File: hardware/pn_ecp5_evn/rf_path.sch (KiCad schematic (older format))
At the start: 37 parts, among them J701 Conn_Coaxial, J702 Conn_Coaxial, J703 Conn_Coaxial, U701 SYM-63LH+, U702 ADG621, U703 OPA2211

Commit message: first pass footprint assignment on pn r0
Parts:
- C701, C702, C703, C704, C705, C706, C707, C708, C709, C710, C711, C712: footprint (none) -> Capacitor_SMD:C_0402_1005Metric
- J701, J702, J703: footprint (none) -> Connector_Coaxial:U.FL_Hirose_U.FL-R-SMT-1_Vertical
- R701, R702, R703, R704, R705, R706, R707, R708, R709, R710, R711, R712, R713, R714, R715, R716, R717, R718, R719: footprint (none) -> Resistor_SMD:R_0402_1005Metric
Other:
- moved on the sheet: U702A, U702C
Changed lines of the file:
@@
 F 0 "C701" V 1621 3200 50  0000 C CNN
 F 1 "C_Small" V 1712 3200 50  0000 C CNN
-F 2 "" H 1850 3200 50  0001 C CNN
+F 2 "Capacitor_SMD:C_0402_1005Metric" H 1850 3200 50  0001 C CNN
 F 3 "~" H 1850 3200 50  0001 C CNN
 	1    1850 3200
@@
 F 0 "C703" H 2658 4354 50  0000 R CNN
 F 1 "DNI" H 2658 4445 50  0000 R CNN
-F 2 "" H 2750 4400 50  0001 C CNN
+F 2 "Capacitor_SMD:C_0402_1005Metric" H 2750 4400 50  0001 C CNN
 F 3 "~" H 2750 4400 50  0001 C CNN
 	1    2750 4400
@@
 F 0 "C702" H 2658 4146 50  0000 R CNN
 F 1 "DNI" H 2658 4055 50  0000 R CNN
-F 2 "" H 2750 4100 50  0001 C CNN
+F 2 "Capacitor_SMD:C_0402_1005Metric" H 2750 4100 50  0001 C CNN
 F 3 "~" H 2750 4100 50  0001 C CNN
 	1    2750 4100
@@
 F 0 "R702" H 4309 5796 50  0000 L CNN
 F 1 "R_Small" H 4309 5705 50  0000 L CNN
-F 2 "" H 4250 5750 50  0001 C CNN
+F 2 "Resistor_SMD:R_0402_1005Metric" H 4250 5750 50  0001 C CNN
 F 3 "~" H 4250 5750 50  0001 C CNN
 	1    4250 5750
@@
 F 0 "C710" H 4908 6154 50  0000 R CNN
 F 1 "C_Small" H 4908 6245 50  0000 R CNN
-F 2 "" H 5000 6200 50  0001 C CNN
+F 2 "Capacitor_SMD:C_0402_1005Metric" H 5000 6200 50  0001 C CNN
 F 3 "~" H 5000 6200 50  0001 C CNN
 	1    5000 6200
@@
 F 0 "C709" H 4408 6154 50  0000 R CNN
 F 1 "C_Small" H 4408 6245 50  0000 R CNN
-F 2 "" H 4500 6200 50  0001 C CNN
+F 2 "Capacitor_SMD:C_0402_1005Metric" H 4500 6200 50  0001 C CNN
 F 3 "~" H 4500 6200 50  0001 C CNN
 	1    4500 6200
@@
 F 0 "C708" H 4358 7154 50  0000 R CNN
 F 1 "C_Small" H 4358 7245 50  0000 R CNN
-F 2 "" H 4450 7200 50  0001 C CNN
+F 2 "Capacitor_SMD:C_0402_1005Metric" H 4450 7200 50  0001 C CNN
 F 3 "~" H 4450 7200 50  0001 C CNN
 	1    4450 7200
@@
 F 0 "R719" V 8254 2450 50  0000 C CNN
 F 1 "R_Small" V 8345 2450 50  0000 C CNN
-F 2 "" H 8450 2450 50  0001 C CNN
+F 2 "Resistor_SMD:R_0402_1005Metric" H 8450 2450 50  0001 C CNN
 F 3 "~" H 8450 2450 50  0001 C CNN
 	1    8450 2450
@@
 F 0 "R701" H 3791 2804 50  0000 R CNN
 F 1 "R_Small" H 3791 2895 50  0000 R CNN
-F 2 "" H 3850 2850 50  0001 C CNN
+F 2 "Resistor_SMD:R_0402_1005Metric" H 3850 2850 50  0001 C CNN
 F 3 "~" H 3850 2850 50  0001 C CNN
 	1    3850 2850
@@
 F 0 "J702" H 4300 2325 50  0000 L CNN
 F 1 "Conn_Coaxial" H 4300 2234 50  0000 L CNN
-F 2 "" H 4200 2350 50  0001 C CNN
+F 2 "Connector_Coaxial:U.FL_Hirose_U.FL-R-SMT-1_Vertical" H 4200 2350 50  0001 C CNN
 F 3 " ~" H 4200 2350 50  0001 C CNN
 	1    4200 2350
@@
 F 0 "R716" V 8054 4200 50  0000 C CNN
 F 1 "R_Small" V 8145 4200 50  0000 C CNN
-F 2 "" H 8250 4200 50  0001 C CNN
+F 2 "Resistor_SMD:R_0402_1005Metric" H 8250 4200 50  0001 C CNN
 F 3 "~" H 8250 4200 50  0001 C CNN
 	1    8250 4200
@@
 F 0 "R714" V 7754 4500 50  0000 C CNN
 F 1 "R_Small" V 7845 4500 50  0000 C CNN
-F 2 "" H 7950 4500 50  0001 C CNN
+F 2 "Resistor_SMD:R_0402_1005Metric" H 7950 4500 50  0001 C CNN
 F 3 "~" H 7950 4500 50  0001 C CNN
 	1    7950 4500
@@
 F 0 "R713" V 7554 4200 50  0000 C CNN
 F 1 "R_Small" V 7645 4200 50  0000 C CNN
-F 2 "" H 7750 4200 50  0001 C CNN
+F 2 "Resistor_SMD:R_0402_1005Metric" H 7750 4200 50  0001 C CNN
 F 3 "~" H 7750 4200 50  0001 C CNN
 	1    7750 4200
@@
 F 0 "C712" H 7258 4504 50  0000 R CNN
 F 1 "DNI" H 7258 4595 50  0000 R CNN
-F 2 "" H 7350 4550 50  0001 C CNN
+F 2 "Capacitor_SMD:C_0402_1005Metric" H 7350 4550 50  0001 C CNN
 F 3 "~" H 7350 4550 50  0001 C CNN
 	1    7350 4550
@@
 F 0 "R712" V 6304 4200 50  0000 C CNN
 F 1 "R_Small" V 6395 4200 50  0000 C CNN
-F 2 "" H 6500 4200 50  0001 C CNN
+F 2 "Resistor_SMD:R_0402_1005Metric" H 6500 4200 50  0001 C CNN
 F 3 "~" H 6500 4200 50  0001 C CNN
 	1    6500 4200
@@
 F 0 "R711" V 6254 3300 50  0000 C CNN
 F 1 "R_Small" V 6345 3300 50  0000 C CNN
-F 2 "" H 6450 3300 50  0001 C CNN
+F 2 "Resistor_SMD:R_0402_1005Metric" H 6450 3300 50  0001 C CNN
 F 3 "~" H 6450 3300 50  0001 C CNN
 	1    6450 3300
@@
 F 0 "R710" H 6091 3504 50  0000 R CNN
 F 1 "R_Small" H 6091 3595 50  0000 R CNN
-F 2 "" H 6150 3550 50  0001 C CNN
+F 2 "Resistor_SMD:R_0402_1005Metric" H 6150 3550 50  0001 C CNN
 F 3 "~" H 6150 3550 50  0001 C CNN
 	1    6150 3550
@@
 F 0 "R708" V 5654 3300 50  0000 C CNN
 F 1 "R_Small" V 5745 3300 50  0000 C CNN
-F 2 "" H 5850 3300 50  0001 C CNN
+F 2 "Resistor_SMD:R_0402_1005Metric" H 5850 3300 50  0001 C CNN
 F 3 "~" H 5850 3300 50  0001 C CNN
 	1    5850 3300
@@
 F 0 "R707" V 5346 2800 50  0000 C CNN
 F 1 "R_Small" V 5255 2800 50  0000 C CNN
-F 2 "" H 5150 2800 50  0001 C CNN
+F 2 "Resistor_SMD:R_0402_1005Metric" H 5150 2800 50  0001 C CNN
 F 3 "~" H 5150 2800 50  0001 C CNN
 	1    5150 2800
@@
 F 0 "R703" V 4254 3200 50  0000 C CNN
 F 1 "R_Small" V 4345 3200 50  0000 C CNN
-F 2 "" H 4450 3200 50  0001 C CNN
+F 2 "Resistor_SMD:R_0402_1005Metric" H 4450 3200 50  0001 C CNN
 F 3 "~" H 4450 3200 50  0001 C CNN
 	1    4450 3200
@@
 F 0 "C704" V 3429 4250 50  0000 C CNN
 F 1 "DNI" V 3338 4250 50  0000 C CNN
-F 2 "" H 3200 4250 50  0001 C CNN
+F 2 "Capacitor_SMD:C_0402_1005Metric" H 3200 4250 50  0001 C CNN
 F 3 "~" H 3200 4250 50  0001 C CNN
 	1    3200 4250
@@
 F 0 "J701" H 3628 4488 50  0000 C CNN
 F 1 "Conn_Coaxial" H 3628 4397 50  0000 C CNN
-F 2 "" H 3700 4250 50  0001 C CNN
+F 2 "Connector_Coaxial:U.FL_Hirose_U.FL-R-SMT-1_Vertical" H 3700 4250 50  0001 C CNN
 F 3 " ~" H 3700 4250 50  0001 C CNN
 	1    3700 4250
@@
 F 0 "J703" H 6600 2425 50  0000 L CNN
 F 1 "Conn_Coaxial" H 6600 2334 50  0000 L CNN
-F 2 "" H 6500 2450 50  0001 C CNN
+F 2 "Connector_Coaxial:U.FL_Hirose_U.FL-R-SMT-1_Vertical" H 6500 2450 50  0001 C CNN
 F 3 " ~" H 6500 2450 50  0001 C CNN
 	1    6500 2450
@@
 F 0 "R709" H 6091 2904 50  0000 R CNN
 F 1 "R_Small" H 6091 2995 50  0000 R CNN
-F 2 "" H 6150 2950 50  0001 C CNN
+F 2 "Resistor_SMD:R_0402_1005Metric" H 6150 2950 50  0001 C CNN
 F 3 "~" H 6150 2950 50  0001 C CNN
 	1    6150 2950
@@
 F 0 "R705" V 4946 2100 50  0000 C CNN
 F 1 "R_Small" V 4855 2100 50  0000 C CNN
-F 2 "" H 4750 2100 50  0001 C CNN
+F 2 "Resistor_SMD:R_0402_1005Metric" H 4750 2100 50  0001 C CNN
 F 3 "~" H 4750 2100 50  0001 C CNN
 	1    4750 2100
@@
 F 0 "R706" V 4554 3650 50  0000 C CNN
 F 1 "R_Small" V 4645 3650 50  0000 C CNN
-F 2 "" H 4750 3650 50  0001 C CNN
+F 2 "Resistor_SMD:R_0402_1005Metric" H 4750 3650 50  0001 C CNN
 F 3 "~" H 4750 3650 50  0001 C CNN
 	1    4750 3650
@@
 F 0 "R704" V 4254 3400 50  0000 C CNN
 F 1 "R_Small" V 4345 3400 50  0000 C CNN
-F 2 "" H 4450 3400 50  0001 C CNN
+F 2 "Resistor_SMD:R_0402_1005Metric" H 4450 3400 50  0001 C CNN
 F 3 "~" H 4450 3400 50  0001 C CNN
 	1    4450 3400
@@
 F 0 "C711" V 5379 2450 50  0000 C CNN
 F 1 "DNI" V 5288 2450 50  0000 C CNN
-F 2 "" H 5150 2450 50  0001 C CNN
+F 2 "Capacitor_SMD:C_0402_1005Metric" H 5150 2450 50  0001 C CNN
 F 3 "~" H 5150 2450 50  0001 C CNN
 	1    5150 2450
@@
 F 0 "C707" V 3779 2850 50  0000 C CNN
 F 1 "DNI" V 3688 2850 50  0000 C CNN
-F 2 "" H 3550 2850 50  0001 C CNN
+F 2 "Capacitor_SMD:C_0402_1005Metric" H 3550 2850 50  0001 C CNN
 F 3 "~" H 3550 2850 50  0001 C CNN
 	1    3550 2850
@@
 F 0 "R717" V 8254 1350 50  0000 C CNN
 F 1 "R_Small" V 8345 1350 50  0000 C CNN
-F 2 "" H 8450 1350 50  0001 C CNN
+F 2 "Resistor_SMD:R_0402_1005Metric" H 8450 1350 50  0001 C CNN
 F 3 "~" H 8450 1350 50  0001 C CNN
 	1    8450 1350
@@
 F 0 "R715" V 7954 1000 50  0000 C CNN
 F 1 "R_Small" V 8045 1000 50  0000 C CNN
-F 2 "" H 8150 1000 50  0001 C CNN
+F 2 "Resistor_SMD:R_0402_1005Metric" H 8150 1000 50  0001 C CNN
 F 3 "~" H 8150 1000 50  0001 C CNN
 	1    8150 1000
@@
 F 0 "R718" V 8254 1750 50  0000 C CNN
 F 1 "R_Small" V 8345 1750 50  0000 C CNN
-F 2 "" H 8450 1750 50  0001 C CNN
+F 2 "Resistor_SMD:R_0402_1005Metric" H 8450 1750 50  0001 C CNN
 F 3 "~" H 8450 1750 50  0001 C CNN
 	1    8450 1750
@@
 L vna:ADG621 U702
 U 3 1 5FE4205A
+P 2950 6600
+F 0 "U702" H 2550 6900 50  0000 C CNN
+F 1 "ADG621" H 2550 7000 50  0000 C CNN
+F 2 "Package_SO:MSOP-10_3x3mm_P0.5mm" H 2950 6500 50  0001 C CNN
+F 3 "https://www.analog.com/media/en/technical-documentation/data-sheets/ADG621.pdf" H 2950 6600 50  0001 C CNN
+	3    2950 6600
+	1    0    0    -1
+$EndComp
+$Comp
+L vna:ADG621 U702
+U 1 1 5FE439E0
 P 8000 2450
-F 0 "U702" H 8000 2717 50  0000 C CNN
-F 1 "ADG621" H 8000 2626 50  0000 C CNN
+F 0 "U702" H 7450 2900 50  0000 L CNN
+F 1 "ADG621" H 7450 2800 50  0000 L CNN
 F 2 "Package_SO:MSOP-10_3x3mm_P0.5mm" H 8000 2350 50  0001 C CNN
 F 3 "https://www.analog.com/media/en/technical-documentation/data-sheets/ADG621.pdf" H 8000 2450 50  0001 C CNN
-	3    8000 2450
-	1    0    0    -1
-$EndComp
-$Comp
-L vna:ADG621 U702
-U 1 1 5FE439E0
-P 2950 6600
-F 0 "U702" H 2400 7050 50  0000 L CNN
-F 1 "ADG621" H 2400 6950 50  0000 L CNN
-F 2 "Package_SO:MSOP-10_3x3mm_P0.5mm" H 2950 6500 50  0001 C CNN
-F 3 "https://www.analog.com/media/en/technical-documentation/data-sheets/ADG621.pdf" H 2950 6600 50  0001 C CNN
-	1    2950 6600
+	1    8000 2450
 	1    0    0    -1
 $EndComp
@@
 F 0 "C706" H 3208 7154 50  0000 R CNN
 F 1 "1 uF" H 3208 7245 50  0000 R CNN
-F 2 "" H 3300 7200 50  0001 C CNN
+F 2 "Capacitor_SMD:C_0402_1005Metric" H 3300 7200 50  0001 C CNN
 F 3 "~" H 3300 7200 50  0001 C CNN
 	1    3300 7200
@@
 F 0 "C705" H 3208 5954 50  0000 R CNN
 F 1 "1 uF" H 3208 6045 50  0000 R CNN
-F 2 "" H 3300 6000 50  0001 C CNN
+F 2 "Capacitor_SMD:C_0402_1005Metric" H 3300 6000 50  0001 C CNN
 F 3 "~" H 3300 6000 50  0001 C CNN
 	1    3300 6000

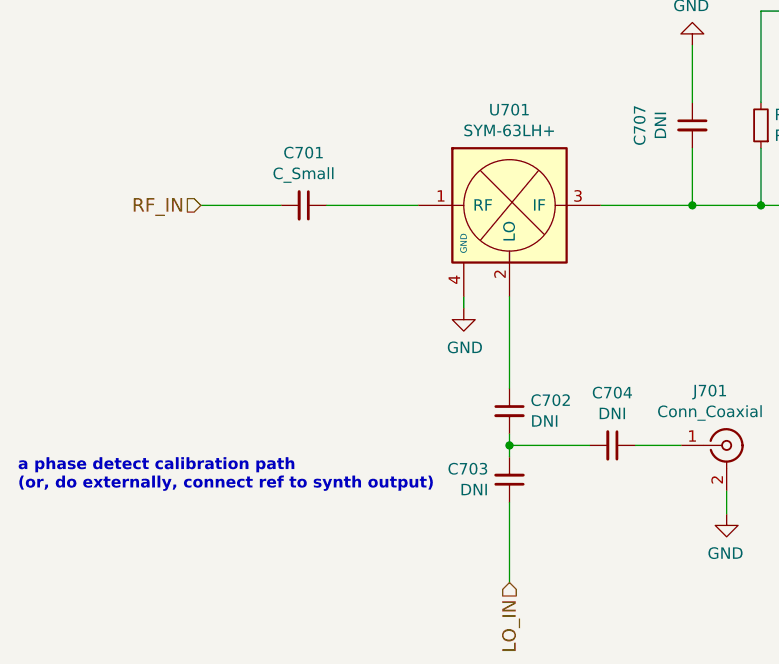
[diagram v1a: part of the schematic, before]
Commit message: started component placement on phase noise analyzer
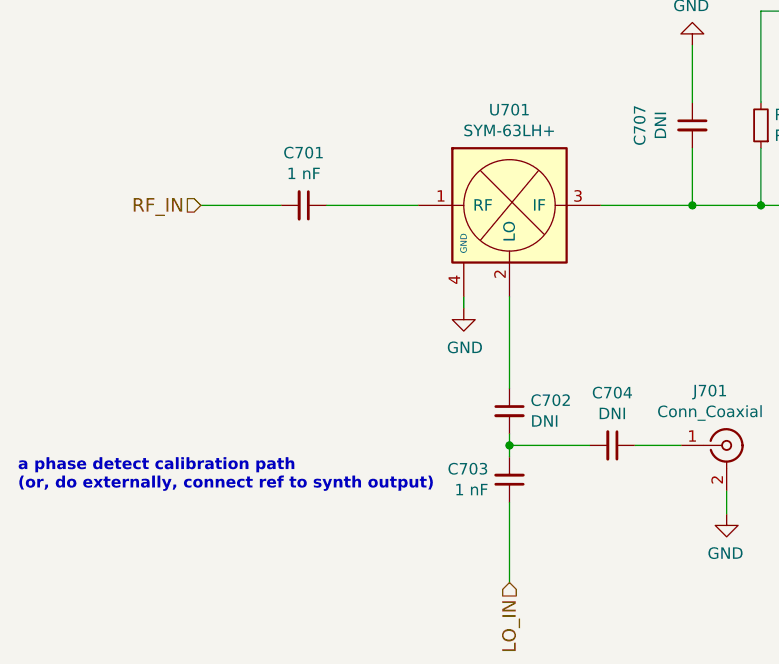
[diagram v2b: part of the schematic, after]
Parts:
- C701: value C_Small -> 1 nF
- C703: value DNI -> 1 nF
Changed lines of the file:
@@
 P 1850 3200
 F 0 "C701" V 1621 3200 50  0000 C CNN
-F 1 "C_Small" V 1712 3200 50  0000 C CNN
+F 1 "1 nF" V 1712 3200 50  0000 C CNN
 F 2 "Capacitor_SMD:C_0402_1005Metric" H 1850 3200 50  0001 C CNN
 F 3 "~" H 1850 3200 50  0001 C CNN
@@
 P 2750 4400
 F 0 "C703" H 2658 4354 50  0000 R CNN
-F 1 "DNI" H 2658 4445 50  0000 R CNN
+F 1 "1 nF" H 2658 4445 50  0000 R CNN
 F 2 "Capacitor_SMD:C_0402_1005Metric" H 2750 4400 50  0001 C CNN
 F 3 "~" H 2750 4400 50  0001 C CNN

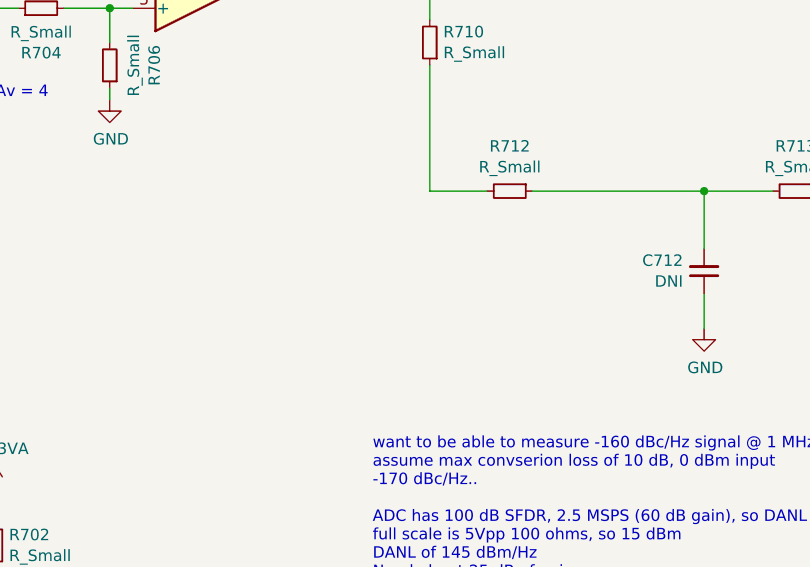
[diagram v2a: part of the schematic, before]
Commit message: work on routing phase noise downconverter
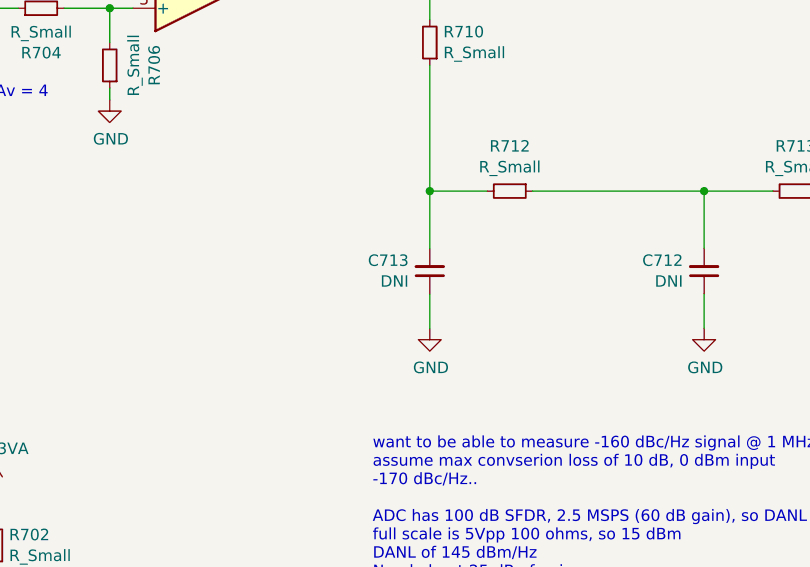
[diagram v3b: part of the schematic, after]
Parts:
- added C713: DNI, Capacitor_SMD:C_0402_1005Metric, symbol Device:C_Small
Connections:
- net GND: now also C713.1
- net at R710.1, R712.2: now also C713.2
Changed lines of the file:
@@
 Wire Wire Line
 	2950 5850 2950 6100
+Wire Wire Line
+	6150 4800 6150 4650
+$Comp
+L power:GND #PWR0305
+U 1 1 5F572A97
+P 6150 4800
+F 0 "#PWR0305" H 6150 4550 50  0001 C CNN
+F 1 "GND" H 6155 4627 50  0000 C CNN
+F 2 "" H 6150 4800 50  0001 C CNN
+F 3 "" H 6150 4800 50  0001 C CNN
+	1    6150 4800
+	1    0    0    -1
+$EndComp
+$Comp
+L Device:C_Small C713
+U 1 1 5F572A9D
+P 6150 4550
+F 0 "C713" H 6058 4504 50  0000 R CNN
+F 1 "DNI" H 6058 4595 50  0000 R CNN
+F 2 "Capacitor_SMD:C_0402_1005Metric" H 6150 4550 50  0001 C CNN
+F 3 "~" H 6150 4550 50  0001 C CNN
+	1    6150 4550
+	1    0    0    1
+$EndComp
+Wire Wire Line
+	6150 4450 6150 4200
+Connection ~ 6150 4200
 $EndSCHEMATC

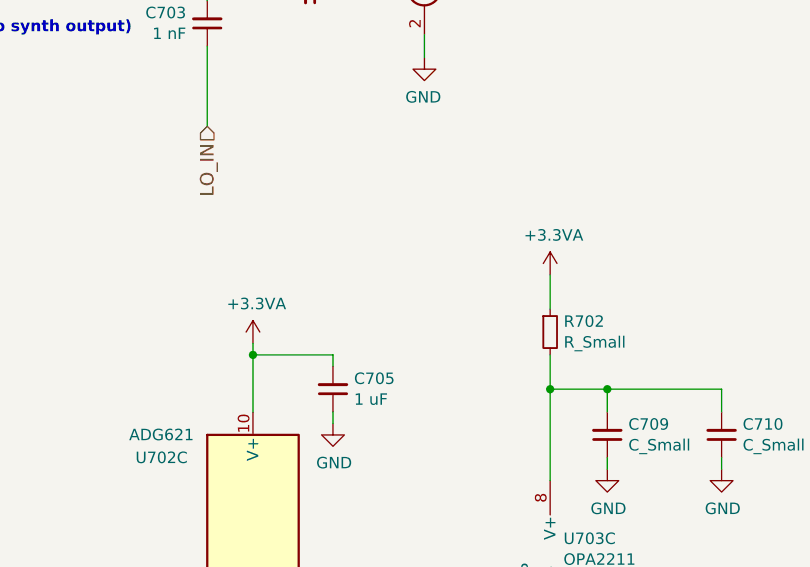
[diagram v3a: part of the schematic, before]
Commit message: layout of phase noise downconverter
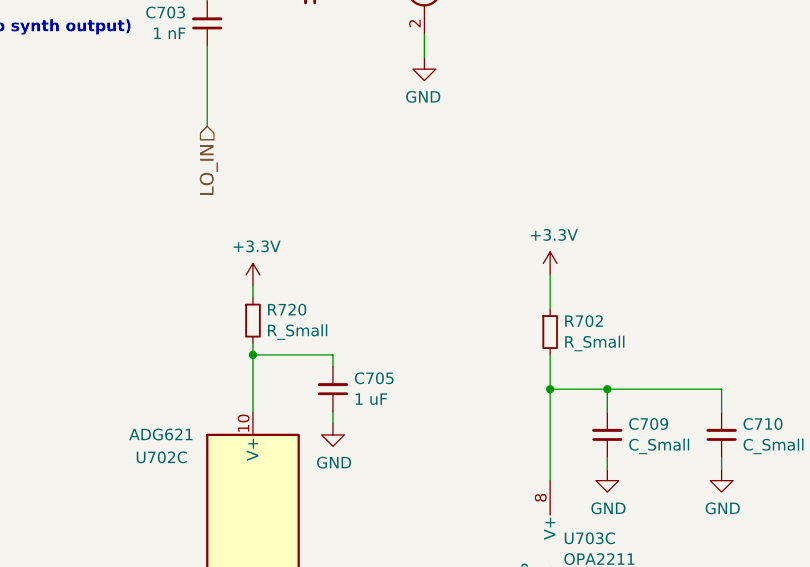
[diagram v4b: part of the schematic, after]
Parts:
- added R720: R_Small, Resistor_SMD:R_0402_1005Metric, symbol Device:R_Small
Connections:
- net +3.3VA: no longer names the net of C705.2, U702.10 (V+)
- net +3.3VA: now also R720.2; no longer R702.1
- new net +3V3: R702.1, R720.1
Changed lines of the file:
@@
 Wire Wire Line
 	4250 5500 4250 5650
-$Comp
-L power:+3.3VA #PWR0220
-U 1 1 5F8805F8
-P 4250 5500
-AR Path="/5F265927/5F8805F8" Ref="#PWR0220"  Part="1"
-AR Path="/5F4ECD93/5F8805F8" Ref="#PWR?"  Part="1"
-F 0 "#PWR0220" H 4250 5350 50  0001 C CNN
-F 1 "+3.3VA" H 4265 5673 50  0000 C CNN
-F 2 "" H 4250 5500 50  0001 C CNN
-F 3 "" H 4250 5500 50  0001 C CNN
-	1    4250 5500
-	1    0    0    -1
-$EndComp
 Connection ~ 4500 6000
 Wire Wire Line
@@
 	8000 2650 8000 2700
 $Comp
-L power:+3.3VA #PWR0234
-U 1 1 606C575F
-P 2950 5800
-AR Path="/5F265927/606C575F" Ref="#PWR0234"  Part="1"
-AR Path="/5F4ECD93/606C575F" Ref="#PWR?"  Part="1"
-F 0 "#PWR0234" H 2950 5650 50  0001 C CNN
-F 1 "+3.3VA" H 2965 5973 50  0000 C CNN
-F 2 "" H 2950 5800 50  0001 C CNN
-F 3 "" H 2950 5800 50  0001 C CNN
-	1    2950 5800
-	1    0    0    -1
-$EndComp
-$Comp
 L power:-3V3 #PWR0235
 U 1 1 606C657B
@@
 	6150 4450 6150 4200
 Connection ~ 6150 4200
+$Comp
+L power:+3.3V #PWR0220
+U 1 1 5F4CD49E
+P 2950 5550
+F 0 "#PWR0220" H 2950 5400 50  0001 C CNN
+F 1 "+3.3V" H 2965 5723 50  0000 C CNN
+F 2 "" H 2950 5550 50  0001 C CNN
+F 3 "" H 2950 5550 50  0001 C CNN
+	1    2950 5550
+	1    0    0    -1
+$EndComp
+$Comp
+L power:+3.3V #PWR0234
+U 1 1 5F4CF28F
+P 4250 5500
+F 0 "#PWR0234" H 4250 5350 50  0001 C CNN
+F 1 "+3.3V" H 4265 5673 50  0000 C CNN
+F 2 "" H 4250 5500 50  0001 C CNN
+F 3 "" H 4250 5500 50  0001 C CNN
+	1    4250 5500
+	1    0    0    -1
+$EndComp
+$Comp
+L Device:R_Small R720
+U 1 1 5F4D9089
+P 2950 5700
+AR Path="/5F265927/5F4D9089" Ref="R720"  Part="1"
+AR Path="/5F4ECD93/5F4D9089" Ref="R?"  Part="1"
+F 0 "R720" H 3009 5746 50  0000 L CNN
+F 1 "R_Small" H 3009 5655 50  0000 L CNN
+F 2 "Resistor_SMD:R_0402_1005Metric" H 2950 5700 50  0001 C CNN
+F 3 "~" H 2950 5700 50  0001 C CNN
+	1    2950 5700
+	1    0    0    -1
+$EndComp
+Wire Wire Line
+	2950 5550 2950 5600
 $EndSCHEMATC

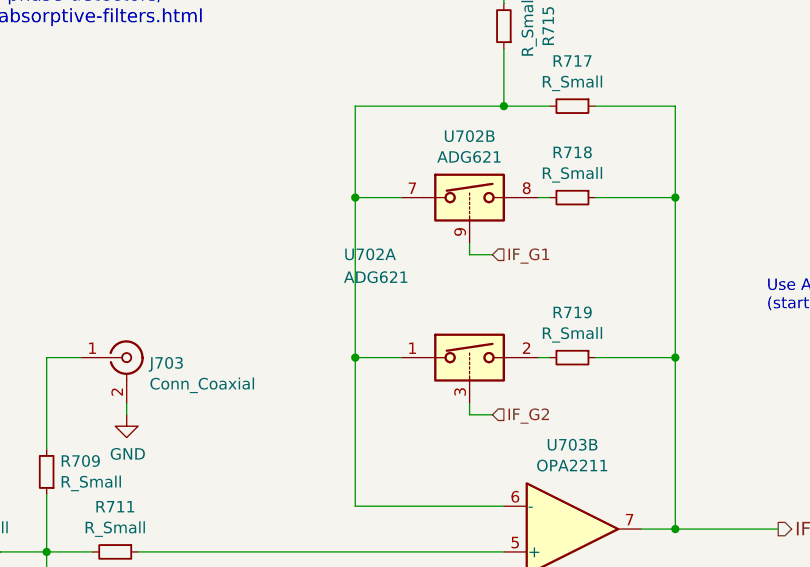
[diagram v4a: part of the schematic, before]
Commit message: drc and erc check, schematic cleanup
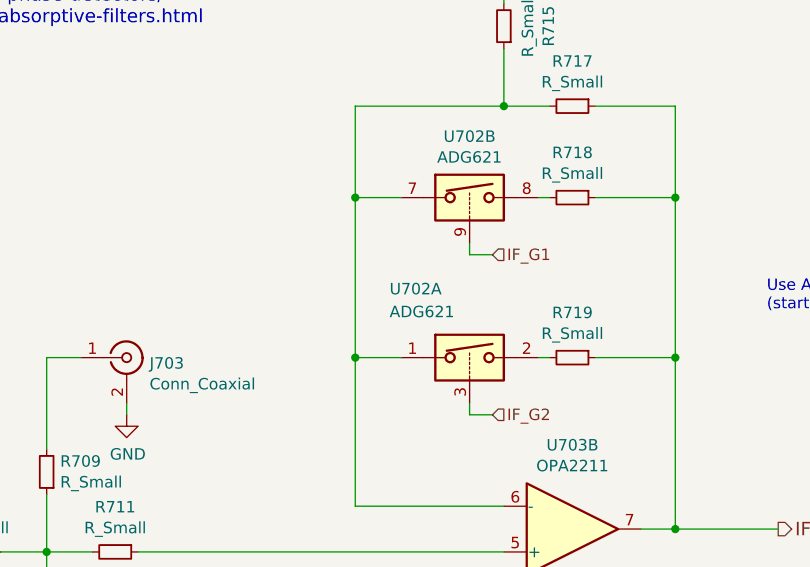
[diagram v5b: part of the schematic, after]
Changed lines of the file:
@@
 U 1 1 5FE439E0
 P 8000 2450
-F 0 "U702" H 7450 2900 50  0000 L CNN
-F 1 "ADG621" H 7450 2800 50  0000 L CNN
+F 0 "U702" H 7650 2750 50  0000 L CNN
+F 1 "ADG621" H 7650 2650 50  0000 L CNN
 F 2 "Package_SO:MSOP-10_3x3mm_P0.5mm" H 8000 2350 50  0001 C CNN
 F 3 "https://www.analog.com/media/en/technical-documentation/data-sheets/ADG621.pdf" H 8000 2450 50  0001 C CNN
